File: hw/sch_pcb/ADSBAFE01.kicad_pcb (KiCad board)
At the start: 2 copper layers, 50.3 x 50.3 mm, 66 parts, among them J1 HEADER_2x02_PARALLEL, J2 HEADER_2x12_PARALLEL, J3 MCX 6GHz 50R, M1 HOLE, M2 HOLE, M3 HOLE, M4 HOLE, M5 RFShield_TwoPieces, SW1 SN74LVC1G3157, SW2 SN74LVC1G3157, U1 BGA2818, U2 AD8313xRM, U3 TLV3542, U4 MCP4017-104E 100k, U5 MCP6566, X1 SF2321D

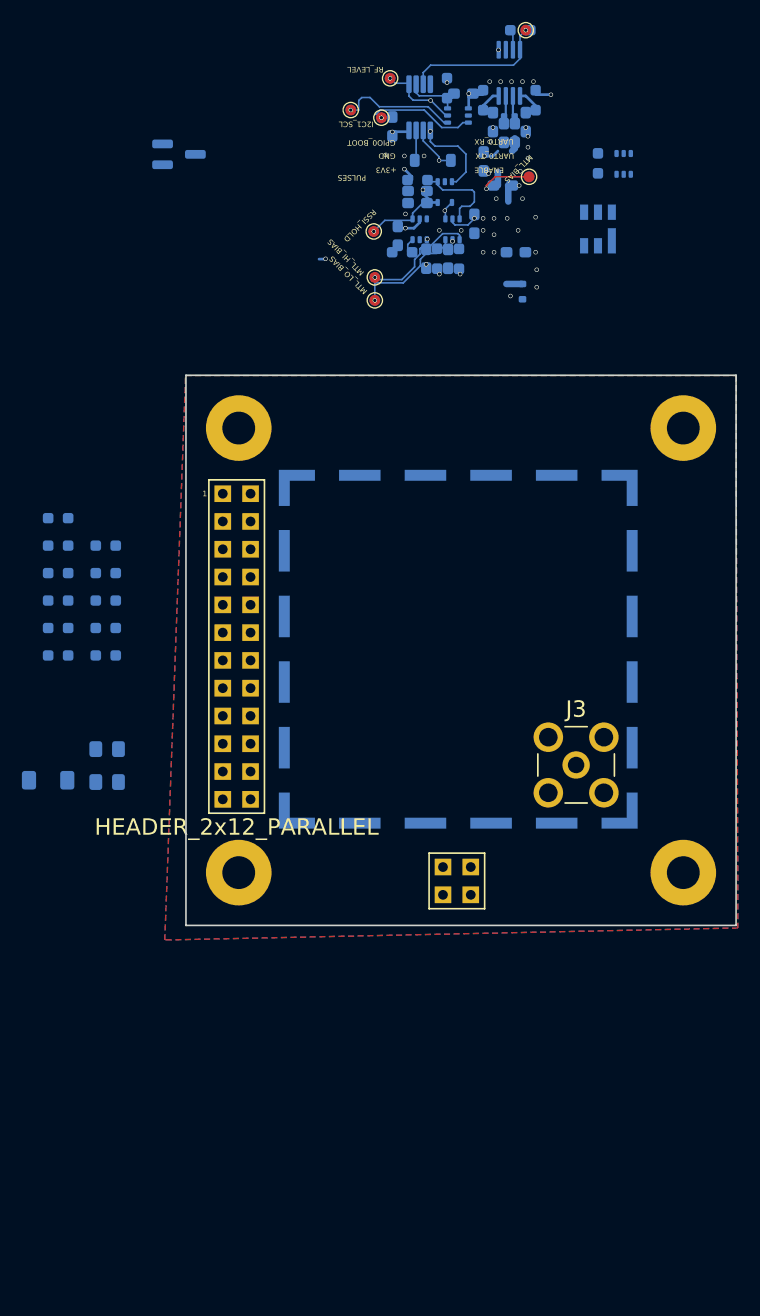
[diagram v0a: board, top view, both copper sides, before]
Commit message: first draft of layout
Parts placement viable. Traces sketched only to test whether connections
are viable.
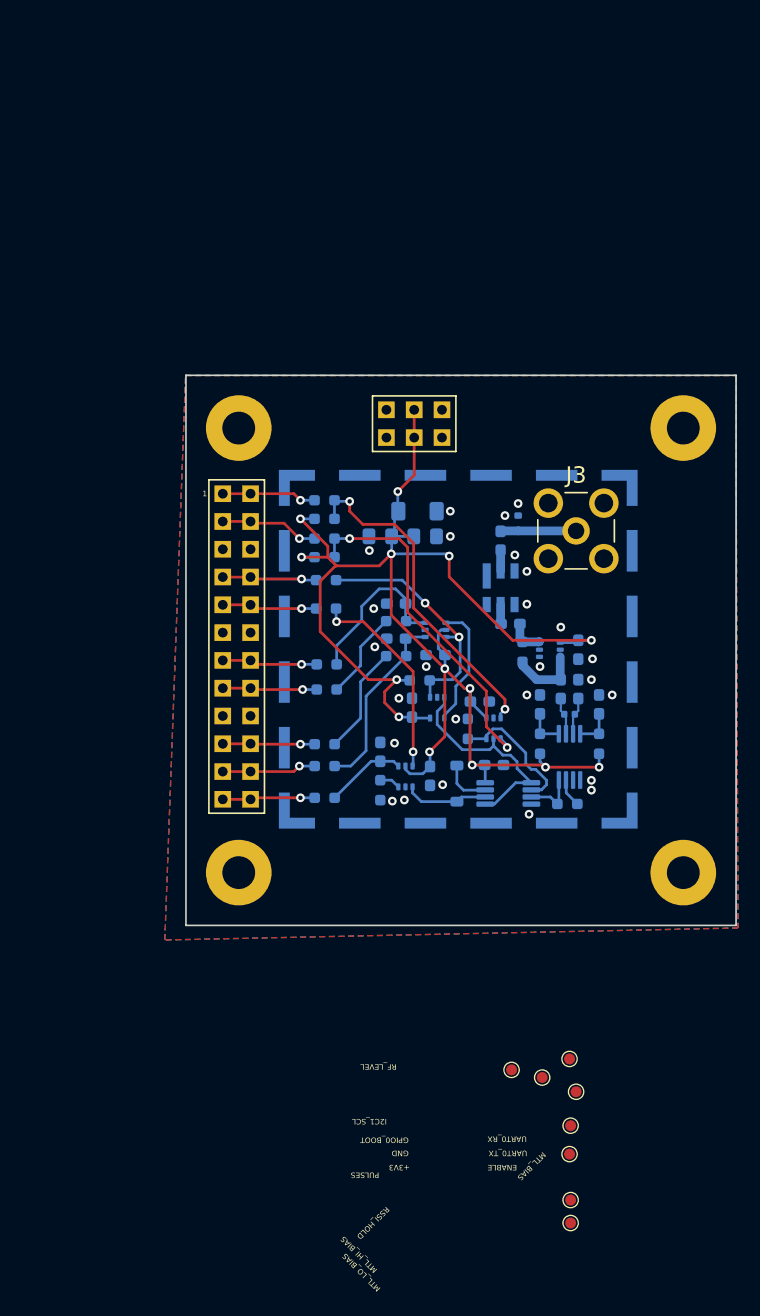
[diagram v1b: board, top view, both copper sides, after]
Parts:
- removed D4: SMP1330-005LF, Package_TO_SOT_SMD:SOT-23_Handsoldering
- removed J1: HEADER_2x02_PARALLEL, Mlab_Pin_Headers:Straight_2x02
- added J4: HEADER_2x03_PARALLEL, Mlab_Pin_Headers:Straight_2x03, F.Cu at (144.2, 84.3)
- moved TP5 94.2 mm to (159.0, 145.4)
- moved TP3 94.1 mm to (158.4, 142.4)
- moved TP6 89.0 mm to (155.9, 144.1)
- moved TP7 89.0 mm to (153.1, 143.4)
- moved TP2 86.8 mm to (158.5, 148.5)
- moved TP1 86.2 mm to (158.5, 157.4)
- moved TP4 86.2 mm to (158.5, 155.3)
- moved TP8 86.2 mm to (158.4, 151.1)
- moved R5 70.9 mm to (158.2, 119.0), turned to 180 degrees
- moved U3 63.2 mm to (152.8, 118.1), turned to 180 degrees
- moved U2 62.8 mm to (158.4, 114.7), turned to -90 degrees
- moved R3 59.8 mm to (161.1, 113.5), turned to 90 degrees
- moved C6 59.1 mm to (151.5, 115.5), turned to 0 degrees
- moved R2 58.8 mm to (155.7, 113.5), turned to 90 degrees
- moved R7 58.6 mm to (149.1, 112.2)
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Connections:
- R14 pad 1: /MTL_LO_PWM -> /MTL_LO_BIAS
- R15 pad 1: /MTL_HI_PWM -> /MTL_LO_PWM
- R16 pad 1: /MTL_LO_BIAS -> /MTL_HI_PWM
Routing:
- net +3V3: track 15.4 -> 141.3 mm, vias 10 -> 14
- net /I2C1_SDA: track 10.8 -> 32.0 mm, vias 1 -> 2
- net /DECODE: track 0.00 -> 18.8 mm, vias 0 -> 2
- net /I2C1_SCL: track 15.9 -> 30.8 mm
- net /PULSES: track 8.36 -> 22.5 mm, vias 0 -> 2
- net /MTL_HI_PWM: track 0.00 -> 10.0 mm, vias 1 -> 0
- net Net-(J2-Pad3): track 0.00 -> 9.03 mm, vias 0 -> 1
- net Net-(J2-Pad13): track 0.00 -> 8.74 mm, vias 0 -> 1
- net Net-(J2-Pad10): track 0.00 -> 8.67 mm, vias 0 -> 1
- net Net-(J2-Pad7): track 0.00 -> 8.65 mm, vias 0 -> 1
- net Net-(J2-Pad15): track 0.00 -> 8.64 mm, vias 0 -> 1
- net Net-(J2-Pad21): track 0.00 -> 8.61 mm, vias 0 -> 1
- net Net-(J2-Pad1): track 0.00 -> 8.54 mm, vias 0 -> 1
- net Net-(J2-Pad23): track 0.00 -> 8.46 mm, vias 0 -> 1
- net Net-(J2-Pad19): track 0.00 -> 8.42 mm, vias 0 -> 1
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
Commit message: Layout done, silk WIP
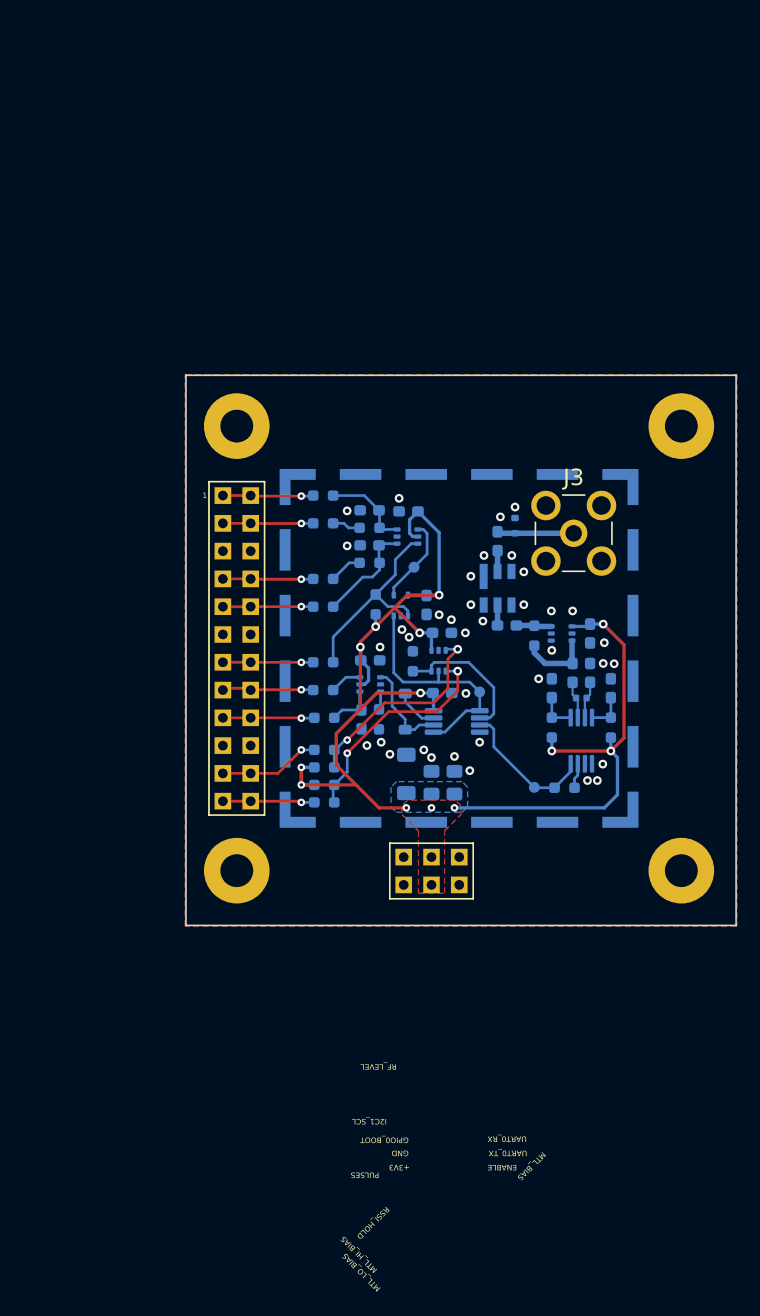
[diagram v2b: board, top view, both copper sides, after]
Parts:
- removed TP1, TP4, TP6, TP7, TP8: TestPoint, TestPoint:TestPoint_Pad_D1.0mm
- TP2, TP3, TP5: moved to B.Cu
- moved TP2 53.0 mm to (144.2, 97.4), turned to 90 degrees
- moved J4 40.9 mm to (145.8, 125.2)
- moved TP5 37.6 mm to (150.2, 108.8)
- moved TP3 25.0 mm to (155.2, 117.5)
- moved R11 24.1 mm to (136.0, 118.9)
- moved D3 24.0 mm to (143.5, 116.3), turned to 90 degrees
- moved C17 23.0 mm to (145.8, 117.1), turned to 90 degrees
- moved R10 22.8 mm to (136.0, 114.1)
- moved R19 22.7 mm to (136.0, 115.7)
- moved C16 22.7 mm to (147.9, 117.1), turned to 90 degrees
- moved R20 20.8 mm to (136.0, 117.3)
- moved R14 15.4 mm to (135.9, 90.8)
- moved R15 15.2 mm to (135.9, 93.4)
- moved R16 15.1 mm to (135.9, 98.5)
- moved R17 14.6 mm to (135.9, 101.0)
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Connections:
- J2 pad 17: GND -> Net-(J2-Pad17)
- J2 pad 18: GND -> Net-(J2-Pad17)
- J2 pad 19: Net-(J2-Pad19) -> GND
- J2 pad 20: Net-(J2-Pad19) -> GND
- R10 pad 2: Net-(J2-Pad1) -> Net-(J2-Pad21)
- R11 pad 2: Net-(J2-Pad3) -> Net-(J2-Pad23)
- R12 pad 2: Net-(J2-Pad7) -> Net-(J2-Pad13)
- R13 pad 2: Net-(J2-Pad10) -> Net-(J2-Pad15)
- R14 pad 2: Net-(J2-Pad13) -> Net-(J2-Pad1)
- R15 pad 2: Net-(J2-Pad15) -> Net-(J2-Pad3)
- R16 pad 2: Net-(J2-Pad19) -> Net-(J2-Pad7)
- R17 pad 2: Net-(J2-Pad21) -> Net-(J2-Pad10)
- R18 pad 2: Net-(J2-Pad23) -> Net-(J2-Pad17)
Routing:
- net +3V3: track 141.3 -> 116.6 mm, vias 14 -> 13
- net /DECODE: track 18.8 -> 2.92 mm, vias 2 -> 0
- net /I2C1_SDA: track 32.0 -> 20.4 mm
- net /I2C1_SCL: track 30.8 -> 19.4 mm
- net Net-(J2-Pad19): track 8.42 -> 0.00 mm, vias 1 -> 0
- net Net-(J2-Pad17): track 0.00 -> 8.38 mm, vias 0 -> 1
- net /RF_DET_OUT: track 4.88 -> 13.0 mm
- net /MTL_HI_BIAS: track 17.1 -> 9.61 mm
- net /MTL_LO_BIAS: track 15.2 -> 8.03 mm
- net /MTL_HI_PWM: track 10.0 -> 3.02 mm
- net /MTL_LO_PWM: track 8.12 -> 2.58 mm
- net /PULSES: track 22.5 -> 18.4 mm, vias 2 -> 0
- net /MTL_BIAS: track 11.4 -> 7.91 mm
- net /RSSI_HOLD: track 7.39 -> 4.54 mm
- net /RF_LEVEL: track 19.9 -> 21.5 mm
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- added copper zone on B.Cu, net +3V3
- added copper zone on F.Cu, net +3V3

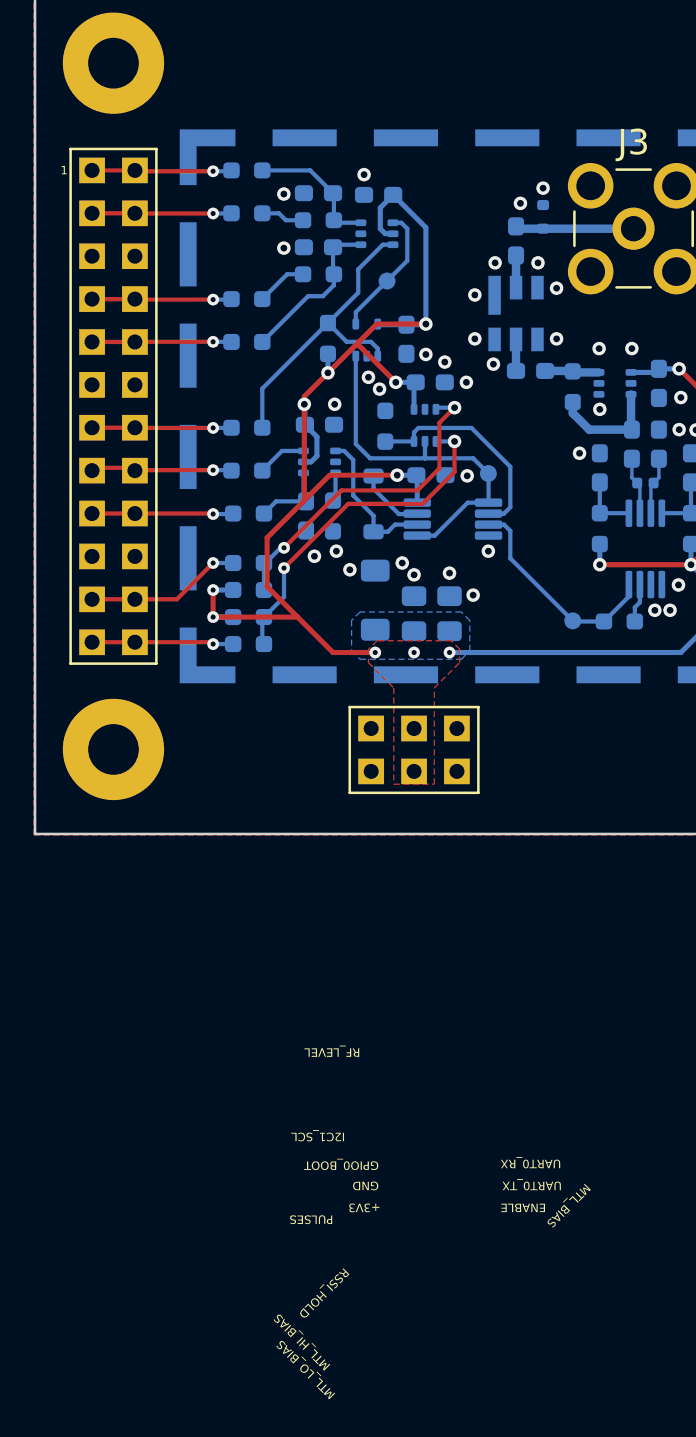
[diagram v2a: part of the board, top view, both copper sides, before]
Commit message: changed footprint U3, silk started
Footprint of U3 changed to edited version which suits clearence 0,2mm.
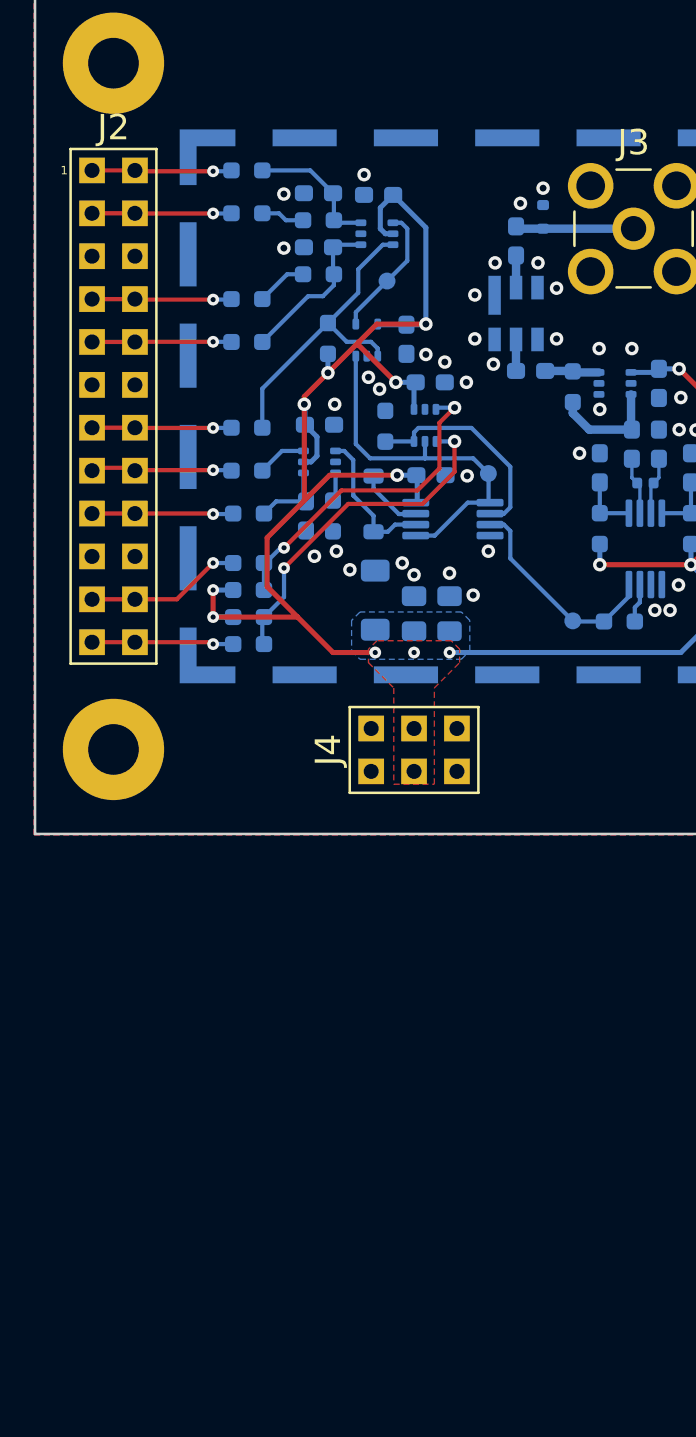
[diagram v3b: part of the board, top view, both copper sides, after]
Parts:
- U3: footprint Package_SO:VSSOP-8_3x3mm_P0.65mm -> ADSB_project_footprints:VSSOP-8_3x3mm_P0.65mm_small
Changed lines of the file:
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@@
 			(at 0 -5.08 90)
 			(layer "F.SilkS")
-			(hide yes)
 			(effects
 				(font
@@
 			(at 0 -16.51 0)
 			(layer "F.SilkS")
-			(hide yes)
 			(effects
 				(font
@@
 			(at 0 1.3 90)
 			(layer "B.SilkS")
-			(hide yes)
 			(effects
 				(font
@@
 		(tags "resistor handsolder")
 		(property "Reference" "R3"
-			(at 0 1.43 90)
+			(at -3.4375 0.3 90)
 			(layer "B.SilkS")
 			(effects
@@
 			(at 0 1.448 0)
 			(layer "B.SilkS")
-			(hide yes)
 			(effects
 				(font
@@
 		(tags "MSOP SO")
 		(property "Reference" "U2"
-			(at 0 2.450001 90)
+			(at 2.3375 2.450001 90)
 			(layer "B.SilkS")
-			(hide yes)
 			(effects
 				(font
@@
 			(at 0 1.448 90)
 			(layer "B.SilkS")
-			(hide yes)
 			(effects
 				(font
@@
 			(at 0 2.000001 0)
 			(layer "B.SilkS")
-			(hide yes)
 			(effects
 				(font
@@
 		)
 	)
-	(footprint "Package_SO:VSSOP-8_3x3mm_P0.65mm"
+	(footprint "ADSB_project_footprints:VSSOP-8_3x3mm_P0.65mm_small"
 		(layer "B.Cu")
 		(at 148.1 111.5 180)
@@
 		)
 		(pad "1" smd roundrect
-			(at -2.1125 0.975 180)
-			(size 1.625 0.5)
+			(at -2.2 0.975 180)
+			(size 1.6 0.45)
 			(layers "B.Cu" "B.Mask" "B.Paste")
 			(roundrect_rratio 0.25)
@@
 		)
 		(pad "2" smd roundrect
-			(at -2.1125 0.325 180)
-			(size 1.625 0.5)
+			(at -2.2 0.325 180)
+			(size 1.6 0.45)
 			(layers "B.Cu" "B.Mask" "B.Paste")
 			(roundrect_rratio 0.25)
@@
 		)
 		(pad "3" smd roundrect
-			(at -2.1125 -0.325 180)
-			(size 1.625 0.5)
+			(at -2.2 -0.325 180)
+			(size 1.6 0.45)
 			(layers "B.Cu" "B.Mask" "B.Paste")
 			(roundrect_rratio 0.25)
@@
 		)
 		(pad "4" smd roundrect
-			(at -2.1125 -0.975 180)
-			(size 1.625 0.5)
+			(at -2.2 -0.975 180)
+			(size 1.6 0.45)
 			(layers "B.Cu" "B.Mask" "B.Paste")
 			(roundrect_rratio 0.25)
@@
 		)
 		(pad "5" smd roundrect
-			(at 2.1125 -0.975 180)
-			(size 1.625 0.5)
+			(at 2.2 -0.975 180)
+			(size 1.6 0.45)
 			(layers "B.Cu" "B.Mask" "B.Paste")
 			(roundrect_rratio 0.25)
@@
 		)
 		(pad "6" smd roundrect
-			(at 2.1125 -0.325 180)
-			(size 1.625 0.5)
+			(at 2.2 -0.325 180)
+			(size 1.6 0.45)
 			(layers "B.Cu" "B.Mask" "B.Paste")
 			(roundrect_rratio 0.25)
@@
 		)
 		(pad "7" smd roundrect
-			(at 2.1125 0.325 180)
-			(size 1.625 0.5)
+			(at 2.2 0.325 180)
+			(size 1.6 0.45)
 			(layers "B.Cu" "B.Mask" "B.Paste")
 			(roundrect_rratio 0.25)
@@
 		)
 		(pad "8" smd roundrect
-			(at 2.1125 0.975 180)
-			(size 1.625 0.5)
+			(at 2.2 0.975 180)
+			(size 1.6 0.45)
 			(layers "B.Cu" "B.Mask" "B.Paste")
 			(roundrect_rratio 0.25)
@@
 		(tags "resistor handsolder")
 		(property "Reference" "R2"
-			(at 0 1.43 90)
+			(at 0.0625 -1.4 90)
 			(layer "B.SilkS")
 			(effects
@@
 		(tags "resistor handsolder")
 		(property "Reference" "R5"
-			(at 0 1.43 0)
+			(at -2.64 -0.5375 0)
 			(layer "B.SilkS")
 			(effects
@@
 			(at 0 2.25 90)
 			(layer "B.SilkS")
-			(hide yes)
 			(effects
 				(font
@@
 			(at 0 2.000001 0)
 			(layer "B.SilkS")
-			(hide yes)
 			(effects
 				(font
@@
 			(at 0 2.25 0)
 			(layer "B.SilkS")
-			(hide yes)
 			(effects
 				(font
@@
 		(tags "test point SMD pad")
 		(property "Reference" "TP3"
-			(at 0 1.448 180)
+			(at 2.2 -0.075 180)
 			(layer "B.SilkS")
-			(hide yes)
 			(effects
 				(font
@@
 			(at 0 2 90)
 			(layer "B.SilkS")
-			(hide yes)
 			(effects
 				(font
@@
 			(at 0 1.17 0)
 			(layer "B.SilkS")
-			(hide yes)
 			(effects
 				(font
@@
 		(tags "capacitor handsolder")
 		(property "Reference" "C4"
-			(at 0 1.43 90)
+			(at 3.3625 0.5 90)
 			(layer "B.SilkS")
 			(effects
@@
 			(at 0 2.000001 90)
 			(layer "B.SilkS")
-			(hide yes)
 			(effects
 				(font
@@
 			(at 0.01 -3.22 90)
 			(layer "B.SilkS")
-			(hide yes)
 			(effects
 				(font
@@
 	)
 	(gr_text "UART0_TX"
-		(at 151.02 150.68 180)
-		(layer "F.SilkS")
+		(at 153.4 146.5 0)
+		(layer "B.SilkS")
 		(effects
 			(font
@@
 				(thickness 0.125)
 			)
-			(justify right bottom)
+			(justify right bottom mirror)
 		)
 	)
 	(gr_text "MTL_HI_BIAS"
-		(at 140.92 161.58 135)
-		(layer "F.SilkS")
+		(at 143.3 135.6 45)
+		(layer "B.SilkS")
 		(effects
 			(font
@@
 				(thickness 0.125)
 			)
-			(justify left bottom)
+			(justify left bottom mirror)
 		)
 	)
 	(gr_text "PULSES"
-		(at 141.02 152.68 180)
-		(layer "F.SilkS")
+		(at 143.4 144.5 0)
+		(layer "B.SilkS")
 		(effects
 			(font
@@
 				(thickness 0.125)
 			)
-			(justify left bottom)
+			(justify left bottom mirror)
 		)
 	)
 	(gr_text "RF_LEVEL"
-		(at 142.62 142.78 180)
-		(layer "F.SilkS")
+		(at 145 154.4 0)
+		(layer "B.SilkS")
 		(effects
 			(font
@@
 				(thickness 0.125)
 			)
-			(justify left bottom)
+			(justify left bottom mirror)
 		)
 	)
 	(gr_text "GPIO0_BOOT"
-		(at 143.72 149.48 180)
-		(layer "F.SilkS")
+		(at 146.1 147.7 0)
+		(layer "B.SilkS")
 		(effects
 			(font
@@
 				(thickness 0.125)
 			)
-			(justify left bottom)
+			(justify left bottom mirror)
 		)
 	)
 	(gr_text "+3V3"
-		(at 143.82 151.98 180)
-		(layer "F.SilkS")
+		(at 146.2 145.2 0)
+		(layer "B.SilkS")
 		(effects
 			(font
@@
 				(thickness 0.125)
 			)
-			(justify left bottom)
+			(justify left bottom mirror)
 		)
 	)
 	(gr_text "GND"
-		(at 143.72 150.68 180)
-		(layer "F.SilkS")
+		(at 146.1 146.5 0)
+		(layer "B.SilkS")
 		(effects
 			(font
@@
 				(thickness 0.125)
 			)
-			(justify left bottom)
+			(justify left bottom mirror)
 		)
 	)
 	(gr_text "RSSI_HOLD"
-		(at 141.62 155.78 225)
-		(layer "F.SilkS")
+		(at 144 141.4 -45)
+		(layer "B.SilkS")
 		(effects
 			(font
@@
 				(thickness 0.125)
 			)
-			(justify left bottom)
+			(justify left bottom mirror)
 		)
 	)
 	(gr_text "ENABLE"
-		(at 150.92 151.98 180)
-		(layer "F.SilkS")
+		(at 153.3 145.2 0)
+		(layer "B.SilkS")
 		(effects
 			(font
@@
 				(thickness 0.125)
 			)
-			(justify right bottom)
+			(justify right bottom mirror)
 		)
 	)
 	(gr_text "MTL_BIAS"
-		(at 155.92 150.78 225)
-		(layer "F.SilkS")
+		(at 158.3 146.4 -45)
+		(layer "B.SilkS")
 		(effects
 			(font
@@
 				(thickness 0.125)
 			)
-			(justify left bottom)
+			(justify left bottom mirror)
 		)
 	)
 	(gr_text "UART0_RX"
-		(at 150.92 149.38 180)
-		(layer "F.SilkS")
+		(at 153.3 147.8 0)
+		(layer "B.SilkS")
 		(effects
 			(font
@@
 				(thickness 0.125)
 			)
-			(justify right bottom)
+			(justify right bottom mirror)
 		)
 	)
 	(gr_text "MTL_LO_BIAS"
-		(at 141.22 163.28 135)
-		(layer "F.SilkS")
+		(at 143.6 133.9 45)
+		(layer "B.SilkS")
 		(effects
 			(font
@@
 				(thickness 0.125)
 			)
-			(justify left bottom)
+			(justify left bottom mirror)
 		)
 	)
 	(gr_text "I2C1_SCL"
-		(at 141.72 147.78 180)
-		(layer "F.SilkS")
+		(at 144.1 149.4 0)
+		(layer "B.SilkS")
 		(effects
 			(font
@@
 				(thickness 0.125)
 			)
-			(justify left bottom)
+			(justify left bottom mirror)
 		)
 	)

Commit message: silk done
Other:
- board text added: "3V3"
- board text added: "DECODE"
- board text added: "I2C_SCL"
- board text added: "I2C_SDA"
- board text added: "MTL_HI_PWM"
- board text added: "MTL_LO_PWM"
- board text removed: "+3V3"
- board text removed: "ENABLE"
- board text removed: "GPIO0_BOOT"
- board text removed: "I2C1_SCL"
- board text removed: "MTL_BIAS"
- board text removed: "RF_LEVEL"
- board text removed: "UART0_RX"
- board text removed: "UART0_TX"

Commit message: reannotated, added 3d model of SAW
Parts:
- renumbered C17 to C1, C8 to C10, C2 to C11, C9 to C12, C10 to C13, C3 to C14, C4 to C15, C13 to C16, C6 to C17, C1 to C2, C11 to C3, C16 to C4, C14 to C6, C12 to C7, C15 to C8, C7 to C9, D3 to D1, D1 to D3, J2 to J1, J4 to J2, M5 to M1, M1 to M2, M2 to M3, M3 to M4, M4 to M5, R19 to R12, R20 to R13, R8 to R14, R6 to R15, R9 to R16, R2 to R17, R3 to R18, R5 to R19, R4 to R2, R7 to R20, R14 to R3, R15 to R4, R16 to R5, R17 to R6, R12 to R7, R13 to R8, R18 to R9, TP5 to TP1, U3 to U1, U5 to U2, U1 to U3, U2 to U4, U4 to U5
